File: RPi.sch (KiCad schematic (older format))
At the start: 3 parts, among them U4 ECP5, X3 RaspberryPiConnector

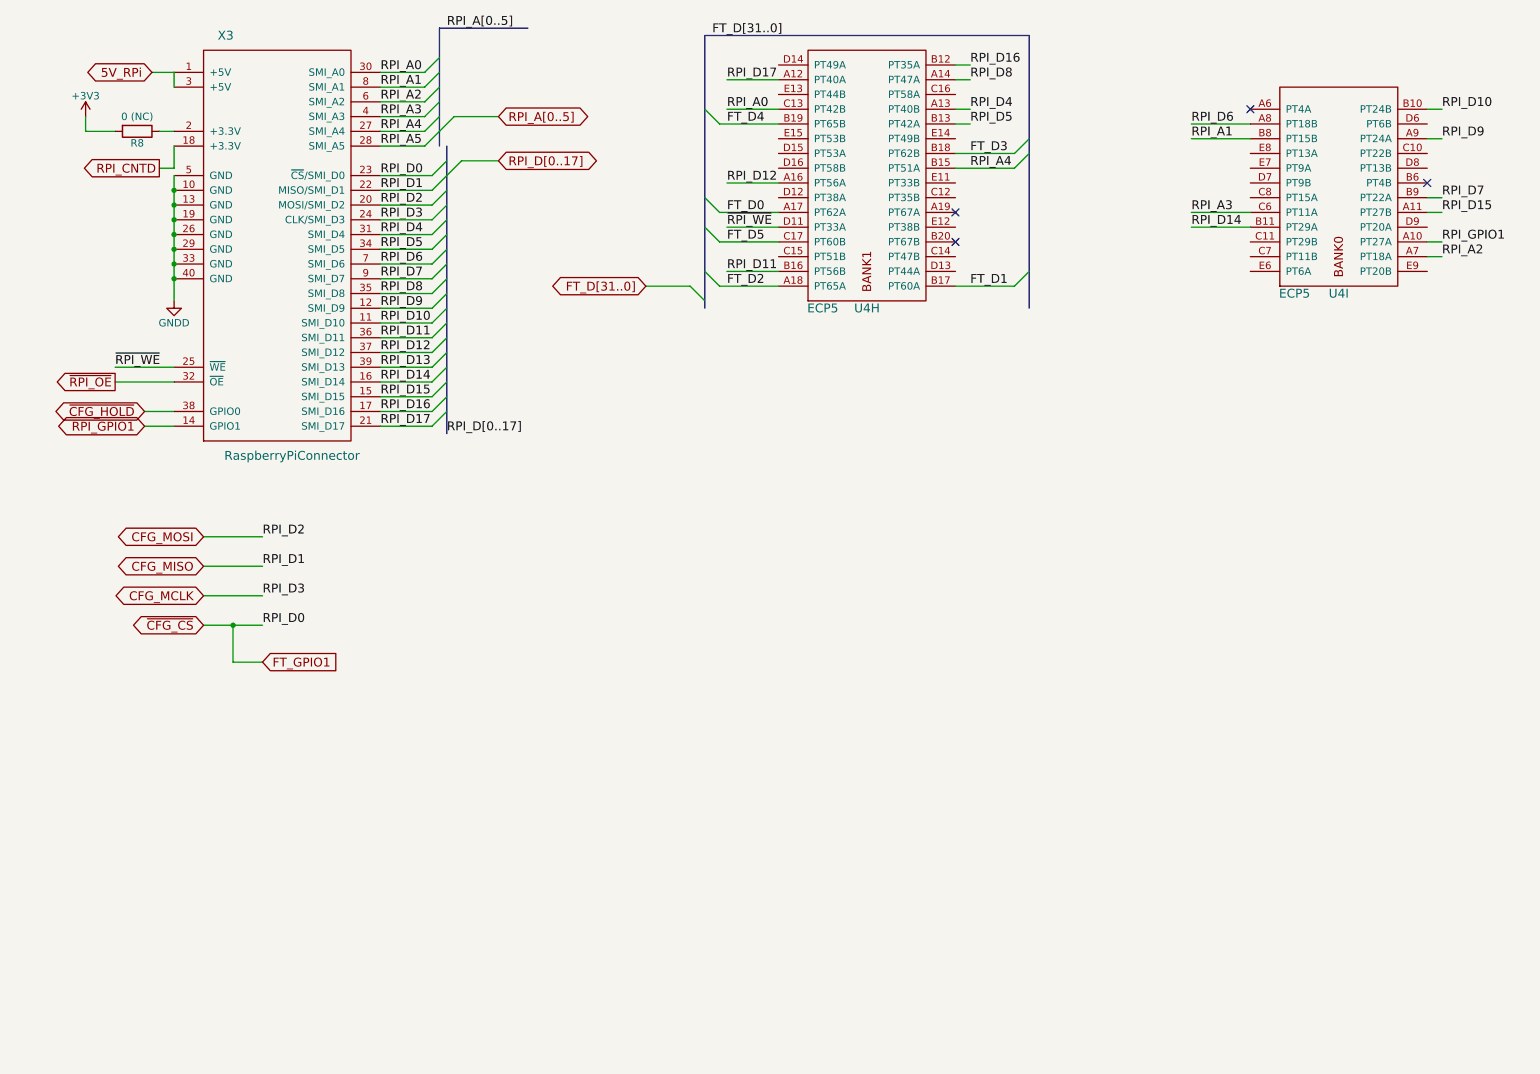
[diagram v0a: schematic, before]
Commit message: Finish tracing all except SDRAM and AFE
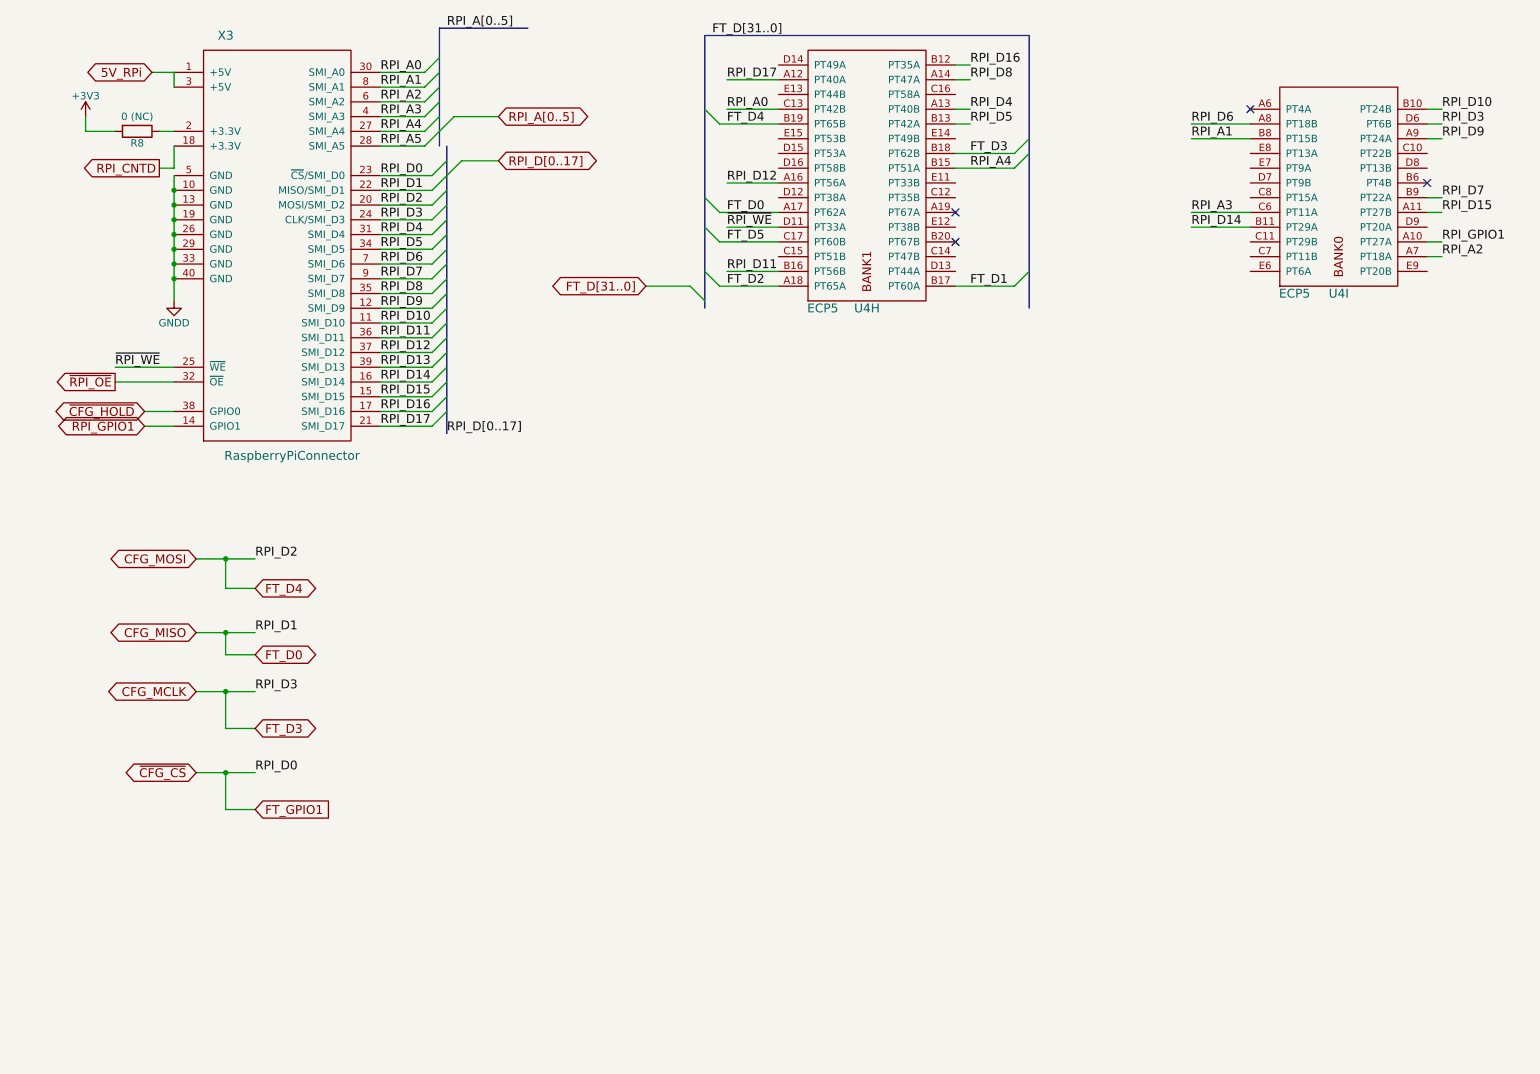
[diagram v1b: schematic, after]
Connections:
- net FT_D0 is gone; now on net CFG_MISO: U4.A17 (PT62A)
- net FT_D3 is gone; now on net CFG_MCLK: U4.B18 (PT62B)
- net FT_D4 is gone; now on net CFG_MOSI: U4.B19 (PT65B)
- net CFG_MCLK: now also U4.D6 (PT6B)
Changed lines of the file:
@@
 Entry Wire Line
 	3250 1650 3350 1550
-Text GLabel 1600 4100 0    60   BiDi ~ 0
+Text GLabel 1550 4250 0    60   BiDi ~ 0
 CFG_MOSI
-Text Label 2000 4100 0    60   ~ 0
+Text Label 1950 4250 0    60   ~ 0
 RPI_D2
-Text GLabel 1600 4300 0    60   BiDi ~ 0
+Text GLabel 1550 4750 0    60   BiDi ~ 0
 CFG_MISO
-Text GLabel 1600 4500 0    60   BiDi ~ 0
+Text GLabel 1550 5150 0    60   BiDi ~ 0
 CFG_MCLK
-Text GLabel 1600 4700 0    60   BiDi ~ 0
+Text GLabel 1550 5700 0    60   BiDi ~ 0
 ~CFG_CS
-Text Label 2000 4700 0    60   ~ 0
+Text Label 1950 5700 0    60   ~ 0
 RPI_D0
-Text Label 2000 4300 0    60   ~ 0
+Text Label 1950 4750 0    60   ~ 0
 RPI_D1
-Text Label 2000 4500 0    60   ~ 0
+Text Label 1950 5150 0    60   ~ 0
 RPI_D3
 Wire Wire Line
@@
 	3350 1550 3600 1550
 Wire Wire Line
-	2000 4100 1600 4100
-Wire Wire Line
-	1600 4300 2000 4300
-Wire Wire Line
-	2000 4500 1600 4500
-Wire Wire Line
-	1600 4700 2000 4700
+	1950 4250 1550 4250
+Wire Wire Line
+	1550 4750 1950 4750
+Wire Wire Line
+	1950 5150 1550 5150
+Wire Wire Line
+	1550 5700 1950 5700
 Wire Bus Line
 	3200 650  3200 1450
@@
 Wire Wire Line
 	5500 2400 5100 2400
-Text GLabel 2000 4950 2    60   Input ~ 0
+Text GLabel 1950 5950 2    60   Input ~ 0
 FT_GPIO1
 Wire Wire Line
-	2000 4950 1800 4950
-Wire Wire Line
-	1800 4950 1800 4700
-Connection ~ 1800 4700
+	1950 5950 1750 5950
+Wire Wire Line
+	1750 5950 1750 5700
+Connection ~ 1750 5700
 Wire Wire Line
 	1000 3050 1400 3050
@@
 Wire Wire Line
 	8700 1900 8300 1900
+Text Label 10000 1300 0    60   ~ 0
+RPI_D3
+Wire Wire Line
+	10000 1300 9900 1300
+Text GLabel 1950 4900 2    60   BiDi ~ 0
+FT_D0
+Wire Wire Line
+	1950 4900 1750 4900
+Wire Wire Line
+	1750 4900 1750 4750
+Connection ~ 1750 4750
+Text GLabel 1950 4450 2    60   BiDi ~ 0
+FT_D4
+Wire Wire Line
+	1950 4450 1750 4450
+Wire Wire Line
+	1750 4450 1750 4250
+Connection ~ 1750 4250
+Text GLabel 1950 5400 2    60   BiDi ~ 0
+FT_D3
+Wire Wire Line
+	1950 5400 1750 5400
+Wire Wire Line
+	1750 5400 1750 5150
+Connection ~ 1750 5150
 $EndSCHEMATC

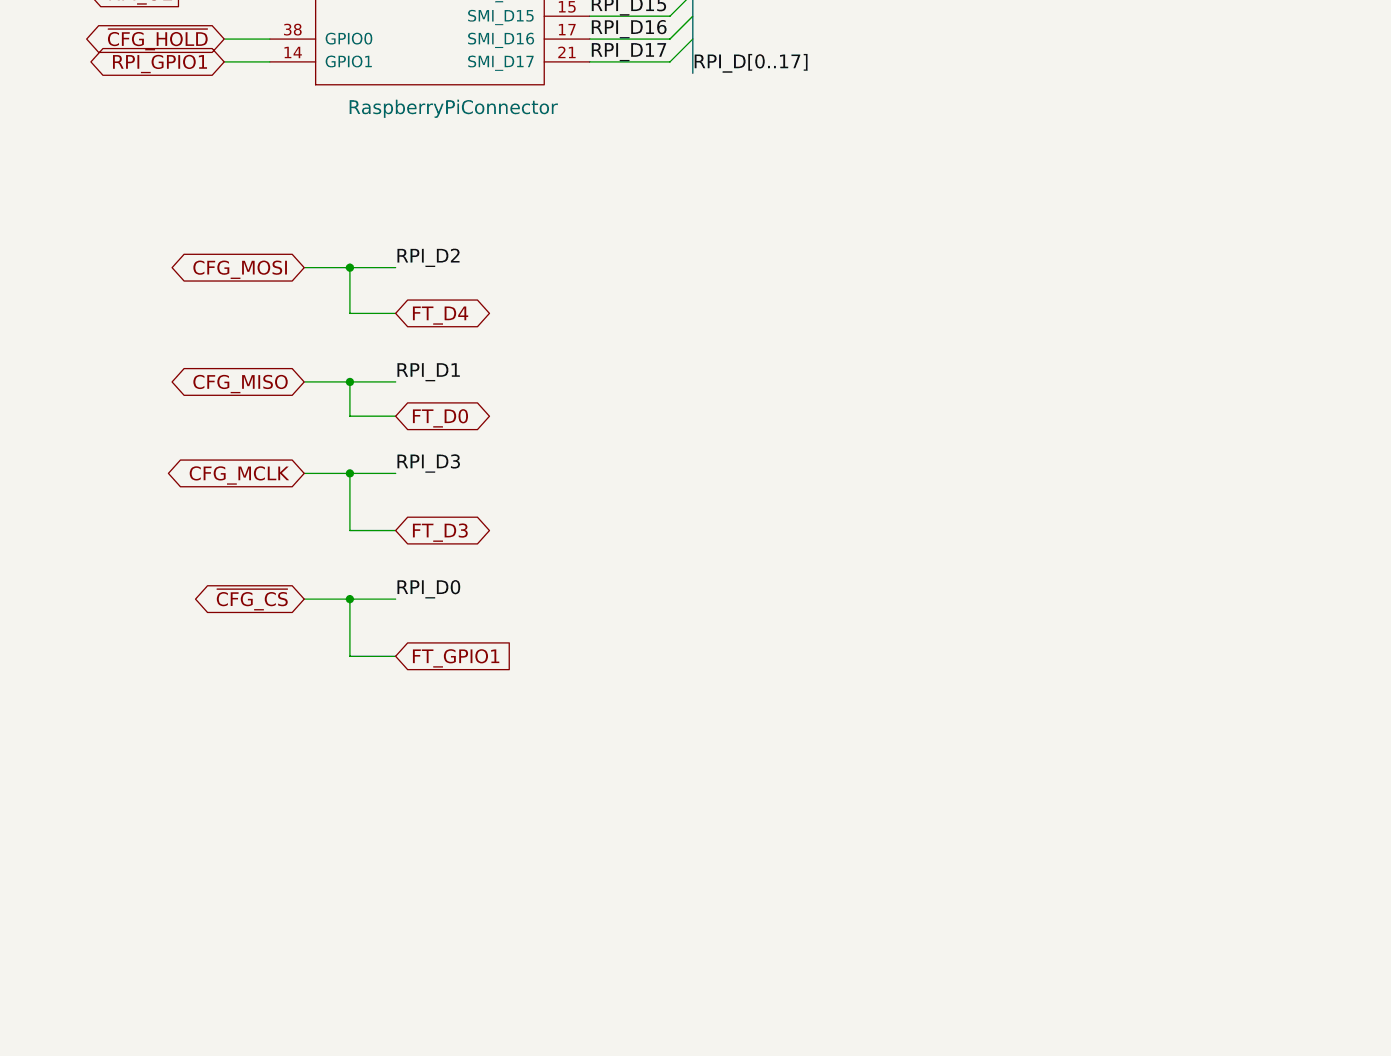
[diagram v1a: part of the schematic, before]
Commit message: Changed RF sheet to add second path to TX and RX
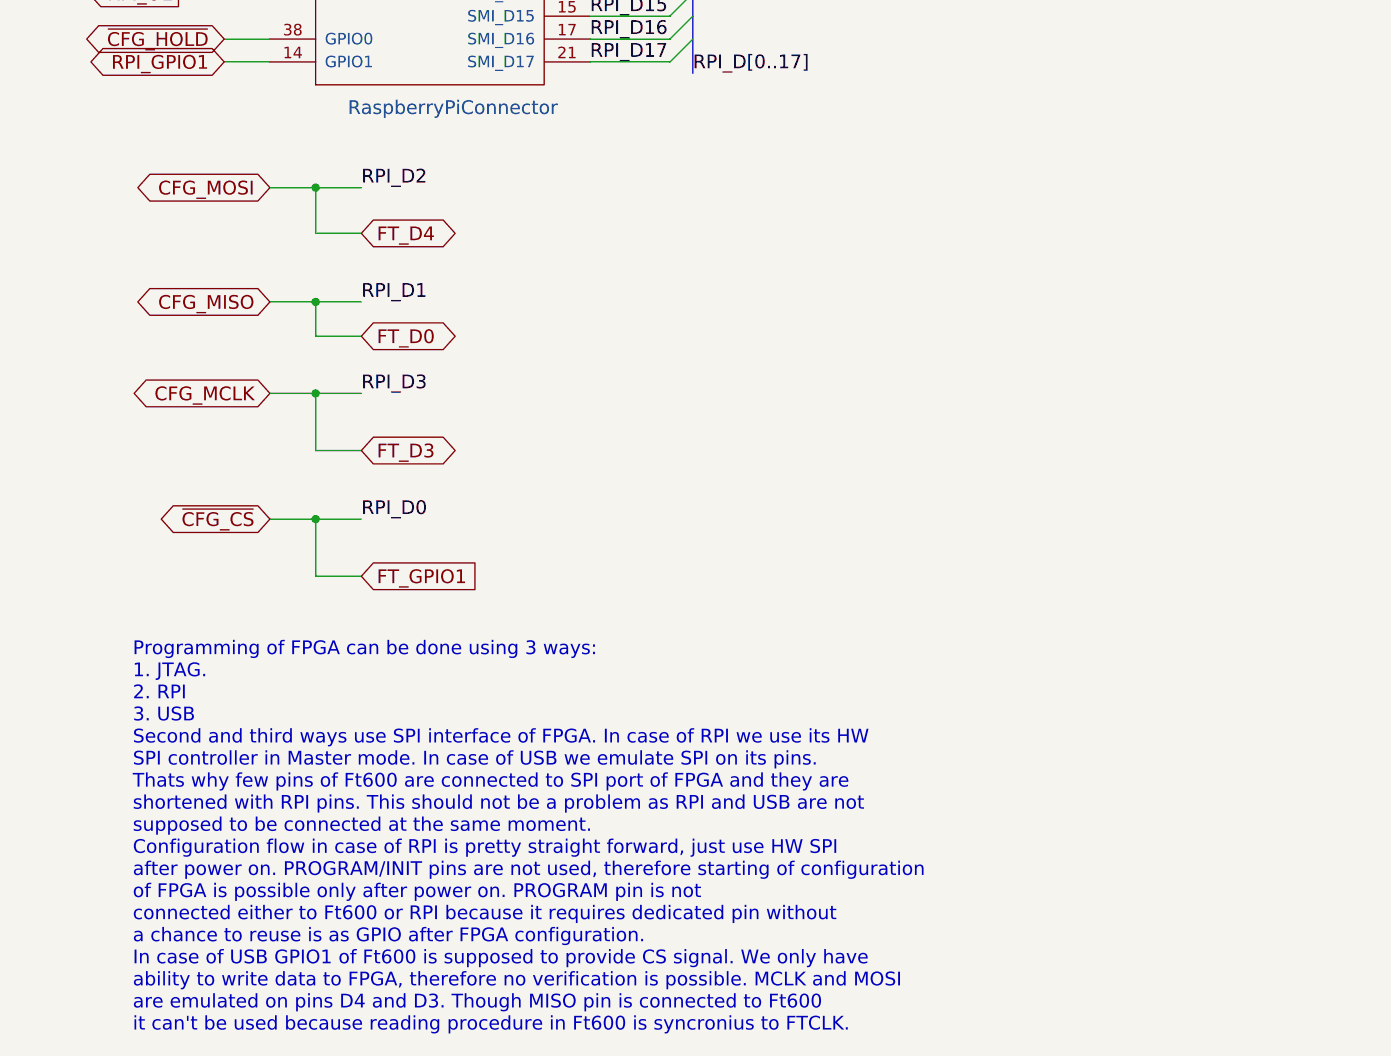
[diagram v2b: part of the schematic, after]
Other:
- note added: "Programming of FPGA can be done using 3 ways:\n1. JTAG. \n2. RPI\n3. USB\nSecond and third ways use SPI interface of FPGA. In case of RPI we use its HW\nSPI controller in Master mode. In case of USB we emulate SPI on its pins.\nThats why few pins of Ft600 are connected to SPI port of FPGA and they are\nshortened with RPI pins. This should not be a problem as RPI and USB are not\nsupposed to be co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"
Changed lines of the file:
@@
 $EndComp
 $Comp
-L +3V3 #PWR037
+L +3V3 #PWR37
 U 1 1 58A418F6
 P 800 1250
-F 0 "#PWR037" H 800 1100 50  0001 C CNN
+F 0 "#PWR37" H 800 1100 50  0001 C CNN
 F 1 "+3V3" H 800 1390 50  0000 C CNN
 F 2 "" H 800 1250 50  0000 C CNN
@@
 $EndComp
 $Comp
-L GNDD #PWR038
+L GNDD #PWR38
 U 1 1 58A80C0C
 P 1400 2500
-F 0 "#PWR038" H 1400 2250 50  0001 C CNN
+F 0 "#PWR38" H 1400 2250 50  0001 C CNN
 F 1 "GNDD" H 1400 2350 50  0000 C CNN
 F 2 "" H 1400 2500 50  0000 C CNN
@@
 Entry Wire Line
 	3250 1650 3350 1550
-Text GLabel 1550 4250 0    60   BiDi ~ 0
+Text GLabel 1400 3900 0    60   BiDi ~ 0
 CFG_MOSI
-Text Label 1950 4250 0    60   ~ 0
+Text Label 1800 3900 0    60   ~ 0
 RPI_D2
-Text GLabel 1550 4750 0    60   BiDi ~ 0
+Text GLabel 1400 4400 0    60   BiDi ~ 0
 CFG_MISO
-Text GLabel 1550 5150 0    60   BiDi ~ 0
+Text GLabel 1400 4800 0    60   BiDi ~ 0
 CFG_MCLK
-Text GLabel 1550 5700 0    60   BiDi ~ 0
+Text GLabel 1400 5350 0    60   BiDi ~ 0
 ~CFG_CS
-Text Label 1950 5700 0    60   ~ 0
+Text Label 1800 5350 0    60   ~ 0
 RPI_D0
-Text Label 1950 4750 0    60   ~ 0
+Text Label 1800 4400 0    60   ~ 0
 RPI_D1
-Text Label 1950 5150 0    60   ~ 0
+Text Label 1800 4800 0    60   ~ 0
 RPI_D3
 Wire Wire Line
@@
 	3350 1550 3600 1550
 Wire Wire Line
-	1950 4250 1550 4250
-Wire Wire Line
-	1550 4750 1950 4750
-Wire Wire Line
-	1950 5150 1550 5150
-Wire Wire Line
-	1550 5700 1950 5700
+	1800 3900 1400 3900
+Wire Wire Line
+	1400 4400 1800 4400
+Wire Wire Line
+	1800 4800 1400 4800
+Wire Wire Line
+	1400 5350 1800 5350
 Wire Bus Line
 	3200 650  3200 1450
@@
 Wire Wire Line
 	5500 2400 5100 2400
-Text GLabel 1950 5950 2    60   Input ~ 0
+Text GLabel 1800 5600 2    60   Input ~ 0
 FT_GPIO1
 Wire Wire Line
-	1950 5950 1750 5950
-Wire Wire Line
-	1750 5950 1750 5700
-Connection ~ 1750 5700
+	1800 5600 1600 5600
+Wire Wire Line
+	1600 5600 1600 5350
+Connection ~ 1600 5350
 Wire Wire Line
 	1000 3050 1400 3050
@@
 Wire Wire Line
 	10000 1300 9900 1300
-Text GLabel 1950 4900 2    60   BiDi ~ 0
+Text GLabel 1800 4550 2    60   BiDi ~ 0
 FT_D0
 Wire Wire Line
-	1950 4900 1750 4900
-Wire Wire Line
-	1750 4900 1750 4750
-Connection ~ 1750 4750
-Text GLabel 1950 4450 2    60   BiDi ~ 0
+	1800 4550 1600 4550
+Wire Wire Line
+	1600 4550 1600 4400
+Connection ~ 1600 4400
+Text GLabel 1800 4100 2    60   BiDi ~ 0
 FT_D4
 Wire Wire Line
-	1950 4450 1750 4450
-Wire Wire Line
-	1750 4450 1750 4250
-Connection ~ 1750 4250
-Text GLabel 1950 5400 2    60   BiDi ~ 0
+	1800 4100 1600 4100
+Wire Wire Line
+	1600 4100 1600 3900
+Connection ~ 1600 3900
+Text GLabel 1800 5050 2    60   BiDi ~ 0
 FT_D3
 Wire Wire Line
-	1950 5400 1750 5400
-Wire Wire Line
-	1750 5400 1750 5150
-Connection ~ 1750 5150
+	1800 5050 1600 5050
+Wire Wire Line
+	1600 5050 1600 4800
+Connection ~ 1600 4800
+Text Notes 800  7600 0    60   ~ 0
+Programming of FPGA can be done using 3 ways:\n1. JTAG. \n2. RPI\n3. USB\nSecond and third ways use SPI interface of FPGA. In case of RPI we use its HW\nSPI controller in Master mode. In case of USB we emulate SPI on its pins.\nThats why few pins of Ft600 are connected to SPI port of FPGA and they are\nshortened with RPI pins. This should not be a problem as RPI and USB are not\nsupposed to be connected at the same moment.\nConfiguration flow in case of RPI is pretty straight forward, just use HW SPI\nafter power on. PROGRAM/INIT pins are not used, therefore starting of configuration \nof FPGA is possible only after power on. PROGRAM pin is not\nconnected either to Ft600 or RPI because it requires dedicated pin without\na chance to reuse is as GPIO after FPGA configuration.\nIn case of USB GPIO1 of Ft600 is supposed to provide CS signal. We only have\nability to write data to FPGA, therefore no verification is possible. MCLK and MOSI \nare emulated on pins D4 and D3. Though MISO pin is connected to Ft600 \nit can't be used because reading procedure in Ft600 is syncronius to FTCLK.\n
 $EndSCHEMATC
